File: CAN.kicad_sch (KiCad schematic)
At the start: 19 parts, among them J12 CAN_In, J13 CAN_Out, U10 ADM3055E, U11 CDSOT23-T24CAN

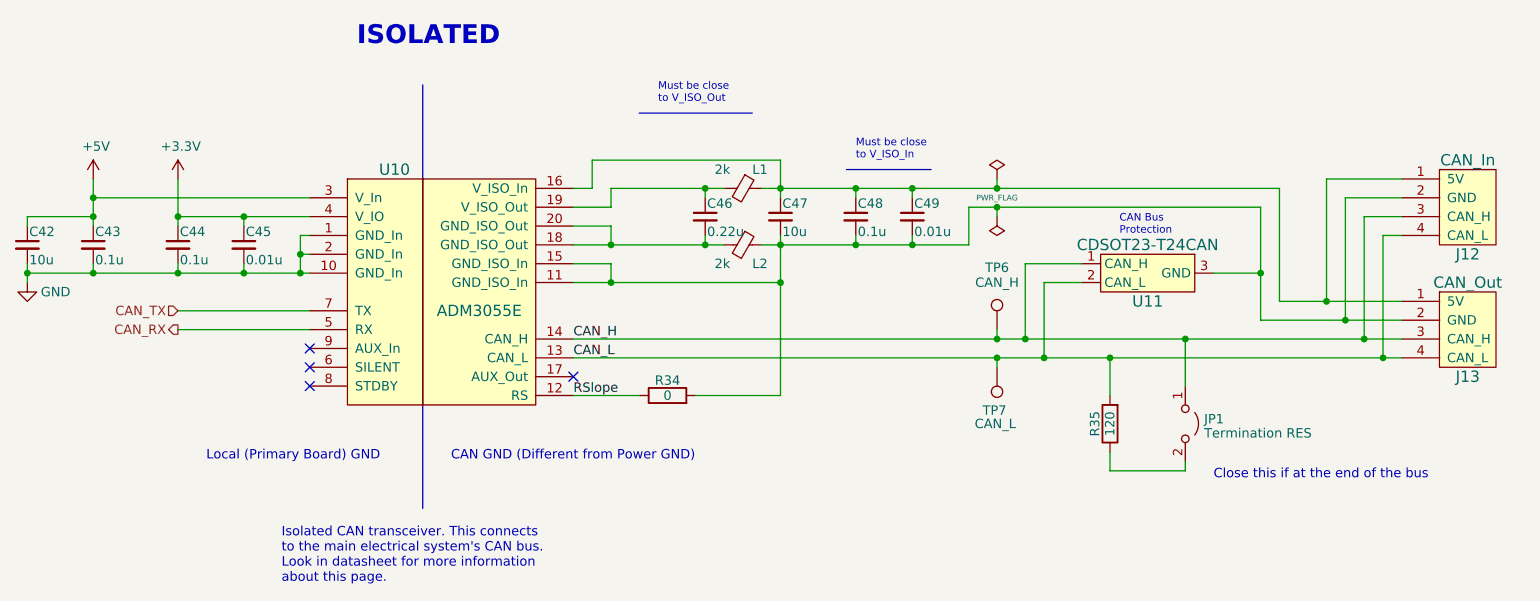
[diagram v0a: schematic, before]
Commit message: bluetooth schematic additions
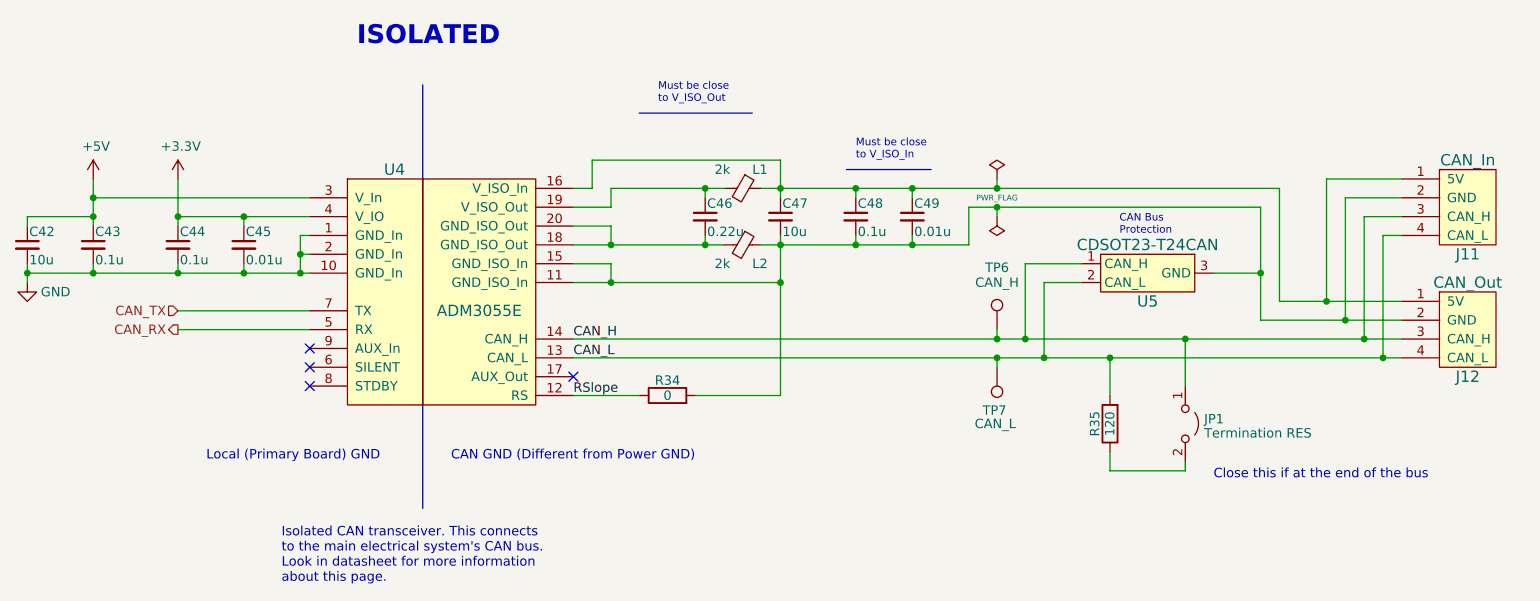
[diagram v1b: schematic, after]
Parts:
- renumbered J12 to J11, J13 to J12, U10 to U4, U11 to U5
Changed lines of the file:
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@@
   (symbol (lib_id "utsvt-connectors:CANConnector") (at 248.92 96.52 0) (mirror y) (unit 1)
     (in_bom yes) (on_board yes) (dnp no)
-    (property "Reference" "J13" (at 248.92 102.87 0)
+    (property "Reference" "J12" (at 248.92 102.87 0)
       (effects (font (size 1.524 1.524)))
     )
@@
       (project "Telemetry-Primary"
         (path "/7f2a449b-14af-42b3-8d38-5f0f8a5ee7ce/00000000-0000-0000-0000-00005f693e58"
-          (reference "J13") (unit 1)
+          (reference "J12") (unit 1)
         )
       )
@@
   (symbol (lib_id "utsvt-chips:ADM3055E") (at 110.49 91.44 0) (unit 1)
     (in_bom yes) (on_board yes) (dnp no)
-    (property "Reference" "U10" (at 104.14 74.93 0)
+    (property "Reference" "U4" (at 104.14 74.93 0)
       (effects (font (size 1.524 1.524)))
     )
@@
       (project "Telemetry-Primary"
         (path "/7f2a449b-14af-42b3-8d38-5f0f8a5ee7ce/00000000-0000-0000-0000-00005f693e58"
-          (reference "U10") (unit 1)
+          (reference "U4") (unit 1)
         )
       )
@@
   (symbol (lib_id "utsvt-chips:CDSOT23-T24CAN") (at 205.74 88.9 0) (unit 1)
     (in_bom yes) (on_board yes) (dnp no)
-    (property "Reference" "U11" (at 205.74 92.71 0)
+    (property "Reference" "U5" (at 205.74 92.71 0)
       (effects (font (size 1.524 1.524)))
     )
@@
       (project "Telemetry-Primary"
         (path "/7f2a449b-14af-42b3-8d38-5f0f8a5ee7ce/00000000-0000-0000-0000-00005f693e58"
-          (reference "U11") (unit 1)
+          (reference "U5") (unit 1)
         )
       )
@@
   (symbol (lib_id "utsvt-connectors:CANConnector") (at 248.92 80.01 0) (mirror y) (unit 1)
     (in_bom yes) (on_board yes) (dnp no)
-    (property "Reference" "J12" (at 248.92 86.36 0)
+    (property "Reference" "J11" (at 248.92 86.36 0)
       (effects (font (size 1.524 1.524)))
     )
@@
       (project "Telemetry-Primary"
         (path "/7f2a449b-14af-42b3-8d38-5f0f8a5ee7ce/00000000-0000-0000-0000-00005f693e58"
-          (reference "J12") (unit 1)
-        )
-      )
+          (reference "J11") (unit 1)
+        )
+      )
